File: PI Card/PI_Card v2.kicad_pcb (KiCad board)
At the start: 4 copper layers, 110 x 75 mm, 22 parts, among them J1 Conn_02x20_Odd_Even, J2 Conn_02x20_Odd_Even, J3 Conn_01x03_Pin, J4 Conn_01x02, J5 Conn_02x40_Odd_Even, J6 Conn_01x03_Pin, SW1 SW_Push

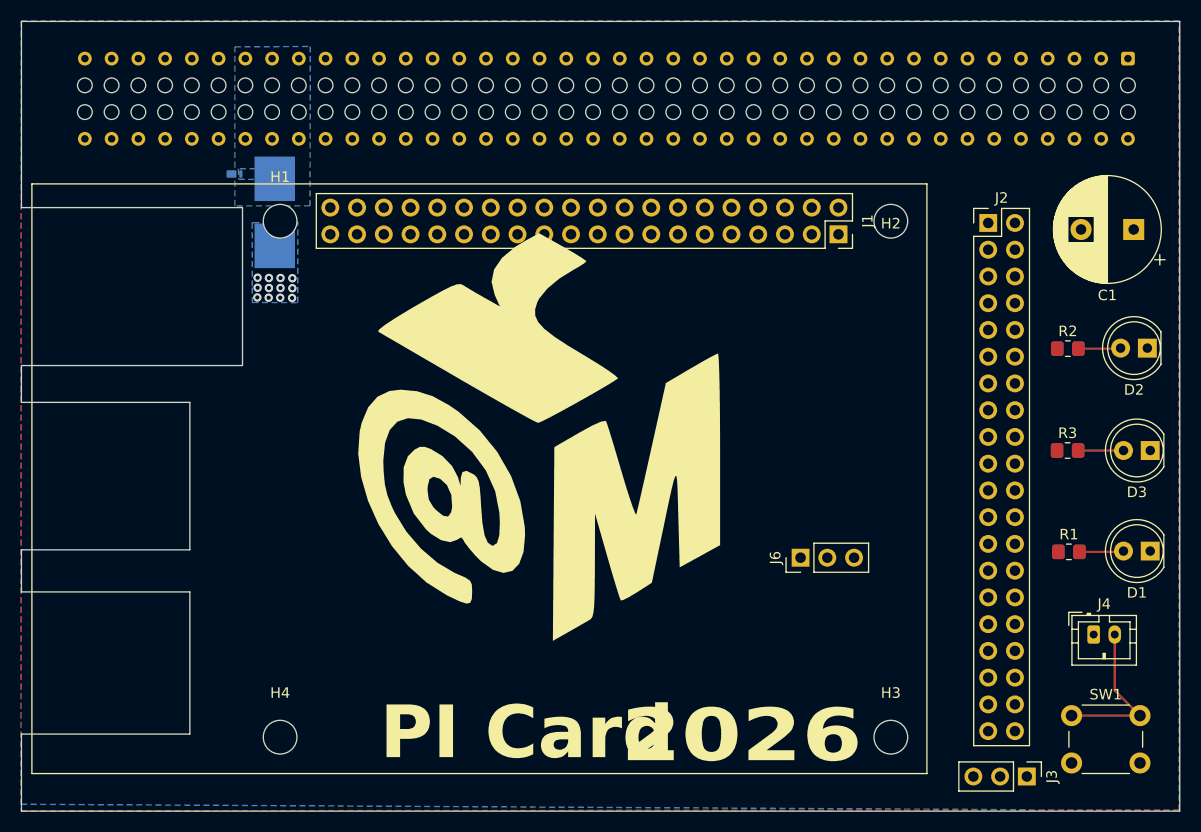
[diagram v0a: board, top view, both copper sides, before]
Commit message: Repositioned Connections
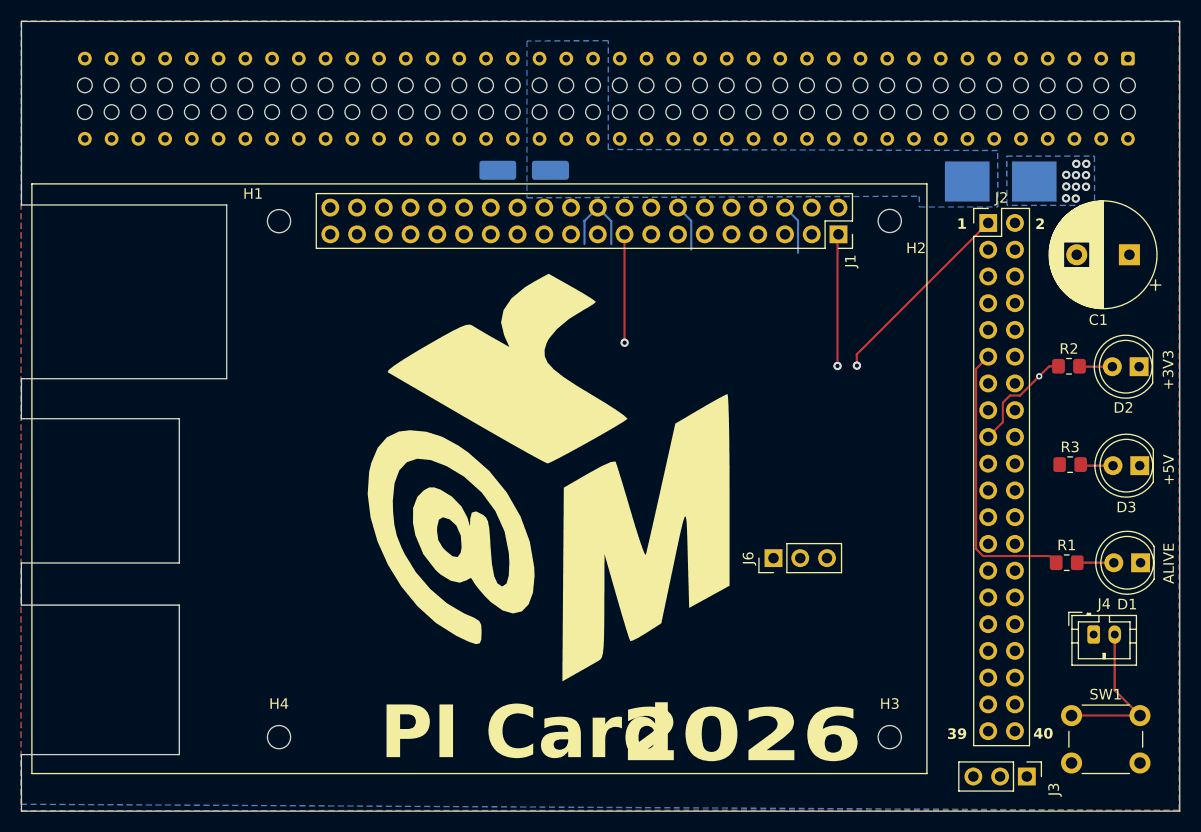
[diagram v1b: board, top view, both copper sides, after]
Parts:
- D4: value PTVS5V0Z1USK -> SMAJ5.0A; footprint Diode_SMD:Nexperia_DSN1608-2_1.6x0.8mm -> Diode_SMD:D_SMA_Handsoldering
- H1, H2, H3, H4: footprint MountingHole:MountingHole_3.2mm_M3 -> MountingHole:MountingHole_2.2mm_M2
- moved F1 69.0 mm to (243.1, 51.7), turned to 180 degrees
- moved D4 27.5 mm to (197.8, 50.6)
- moved G*** 15.0 mm to (200.6, 77.2)
- moved G*** 3.95 mm to (200.2, 79.8)
- moved J6 2.57 mm to (221.5, 87.5)
- moved C1 2.43 mm to (255.3, 58.7)
- moved D2 1.93 mm to (256.2, 69.3)
- moved D3 1.75 mm to (256.3, 78.7)
- moved R2 1.68 mm to (249.6, 69.2)
- moved D1 1.44 mm to (256.4, 87.9)
- moved R3 1.36 mm to (249.7, 78.6)
- moved R1 1.05 mm to (249.4, 87.9)
- moved H2 0.11 mm to (232.6, 55.5)
- moved H1 0.10 mm to (174.6, 55.5)
- moved H3 0.10 mm to (232.6, 104.5)
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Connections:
- J5 pad 1: unconnected-(J5-Pin_1-Pad1) -> GPIO2
- J5 pad 10: GPIO15 -> GPIO24
- J5 pad 11: GPIO17 -> GPIO22
- J5 pad 12: GPIO18 -> GPIO25
- J5 pad 13: GPIO27 -> GPIO10
- J5 pad 14: unconnected-(J5-Pin_14-Pad14) -> GPIO8
- J5 pad 15: GPIO22 -> GPIO9
- J5 pad 16: GPIO23 -> GPIO7
- J5 pad 17: unconnected-(J5-Pin_17-Pad17) -> GPIO11
- J5 pad 18: GPIO24 -> ID_SC
- J5 pad 19: GPIO10 -> ID_SD
- J5 pad 2: unconnected-(J5-Pin_2-Pad2) -> GPIO14
- J5 pad 20: unconnected-(J5-Pin_20-Pad20) -> GPIO12
- J5 pad 21: GPIO9 -> GPIO5
- J5 pad 22: GPIO25 -> GPIO16
- J5 pad 23: GPIO11 -> GPIO6
- J5 pad 24: GPIO8 -> GPIO20
- J5 pad 25: unconnected-(J5-Pin_25-Pad25) -> GPIO13
- J5 pad 26: GPIO7 -> GPIO21
- J5 pad 27: ID_SD -> GPIO19
- J5 pad 28: ID_SC -> unconnected-(J5-Pin_28-Pad28)
- J5 pad 29: GPIO5 -> GPIO26
- J5 pad 3: GPIO2 -> GPIO3
- J5 pad 31: GPIO6 -> unconnected-(J5-Pin_31-Pad31)
- J5 pad 32: GPIO12 -> unconnected-(J5-Pin_32-Pad32)
- J5 pad 33: GPIO13 -> unconnected-(J5-Pin_33-Pad33)
- J5 pad 35: GPIO19 -> unconnected-(J5-Pin_35-Pad35)
- J5 pad 36: GPIO16 -> unconnected-(J5-Pin_36-Pad36)
- J5 pad 37: GPIO26 -> unconnected-(J5-Pin_37-Pad37)
- J5 pad 38: GPIO20 -> unconnected-(J5-Pin_38-Pad38)
- J5 pad 4: unconnected-(J5-Pin_4-Pad4) -> GPIO15
- J5 pad 40: GPIO21 -> unconnected-(J5-Pin_40-Pad40)
- J5 pad 5: GPIO3 -> GPIO4
- J5 pad 6: unconnected-(J5-Pin_6-Pad6) -> GPIO18
- J5 pad 7: GPIO4 -> GPIO17
- J5 pad 8: GPIO14 -> GPIO23
- J5 pad 9: unconnected-(J5-Pin_9-Pad9) -> GPIO27
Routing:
- net +3V3: track 0.00 -> 70.2 mm, vias 0 -> 4
- net GPIO17: track 76.8 -> 111.8 mm
- net GPIO19: track 132.0 -> 152.5 mm
- net GPIO26: track 134.7 -> 154.8 mm
- net GPIO13: track 129.1 -> 149.0 mm
- net GPIO21: track 131.6 -> 150.6 mm
- net GPIO20: track 128.4 -> 146.2 mm
- net GPIO16: track 126.0 -> 143.8 mm
- net GND: track 0.00 -> 17.3 mm
- net GPIO5: track 119.4 -> 134.9 mm
- net GPIO2: track 58.1 -> 43.3 mm
- net GPIO12: track 119.7 -> 134.5 mm
- net GPIO6: track 127.4 -> 141.6 mm
- net ID_SD: track 113.6 -> 126.8 mm
- net GPIO3: track 62.9 -> 49.9 mm
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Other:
- outline, holes or cut-outs redrawn
- board text added: "+3V3"
- board text added: "+5V"
- board text added: "1"
- board text added: "2"
- board text added: "39"
- board text added: "40"
- board text added: "ALIVE"

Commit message: Added I2C & Reset Toggle
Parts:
- added J10: Conn_01x02_Pin, Connector_PinHeader_2.54mm:PinHeader_1x02_P2.54mm_Vertical, F.Cu at (250.9, 66.1)
- added J11: Conn_01x02, Connector_JST:JST_PH_B2B-PH-K_1x02_P2.00mm_Vertical, F.Cu at (248.9, 89.7)
- added J12: Conn_01x02_Pin, Connector_PinHeader_2.54mm:PinHeader_1x02_P2.54mm_Vertical, F.Cu at (257.4, 51.4)
- added J7: Conn_01x02, Connector_JST:JST_PH_B2B-PH-K_1x02_P2.00mm_Vertical, F.Cu at (248.9, 75.4)
- added J8: Conn_01x02, Connector_JST:JST_PH_B2B-PH-K_1x02_P2.00mm_Vertical, F.Cu at (248.9, 96.9)
- added J9: Conn_01x02, Connector_JST:JST_PH_B2B-PH-K_1x02_P2.00mm_Vertical, F.Cu at (248.9, 82.5)
- added SW2: SW_Nidec_CAS-120A1, Button_Switch_SMD:Nidec_Copal_CAS-120A, F.Cu at (255.5, 100.7)
- moved R1 7.45 mm to (255.4, 83.5)
- moved R3 6.23 mm to (255.3, 81.2)
- moved J4 3.01 mm to (254.9, 94.9)
- moved D3 2.11 mm to (256.9, 76.7)
- moved SW1 2.10 mm to (249.8, 104.5)
- moved D2 1.20 mm to (257.3, 68.7)
- moved C1 1.11 mm to (256.4, 59.1)
- moved D1 0.87 mm to (257.2, 88.1)
- moved R2 0.40 mm to (249.2, 69.2)
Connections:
- J4 pad 2: RUN -> Net-(J4-Pin_2)
- SW1 pad 1: RUN -> Net-(J4-Pin_2)
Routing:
- net GND: track 17.3 -> 88.4 mm
- net SCL: track 0.00 -> 54.6 mm
- net SDA: track 0.00 -> 35.5 mm
- net GLOBAL_EN: track 28.2 -> 45.4 mm, vias 0 -> 1
- net Net-(J4-Pin_2): track 0.00 -> 17.1 mm
- net GPIO2: track 43.3 -> 59.0 mm
- net GPIO3: track 49.9 -> 58.9 mm
- net RUN: track 63.5 -> 58.5 mm, vias 0 -> 1
- net Net-(D3-A): track 3.13 -> 5.39 mm
- net Net-(D1-A): track 3.48 -> 5.26 mm
- net Net-(D2-A): track 3.14 -> 4.86 mm
- net GPIO17: track 111.8 -> 113.2 mm
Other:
- board text added: "Global Enable"
- board text added: "RUN"

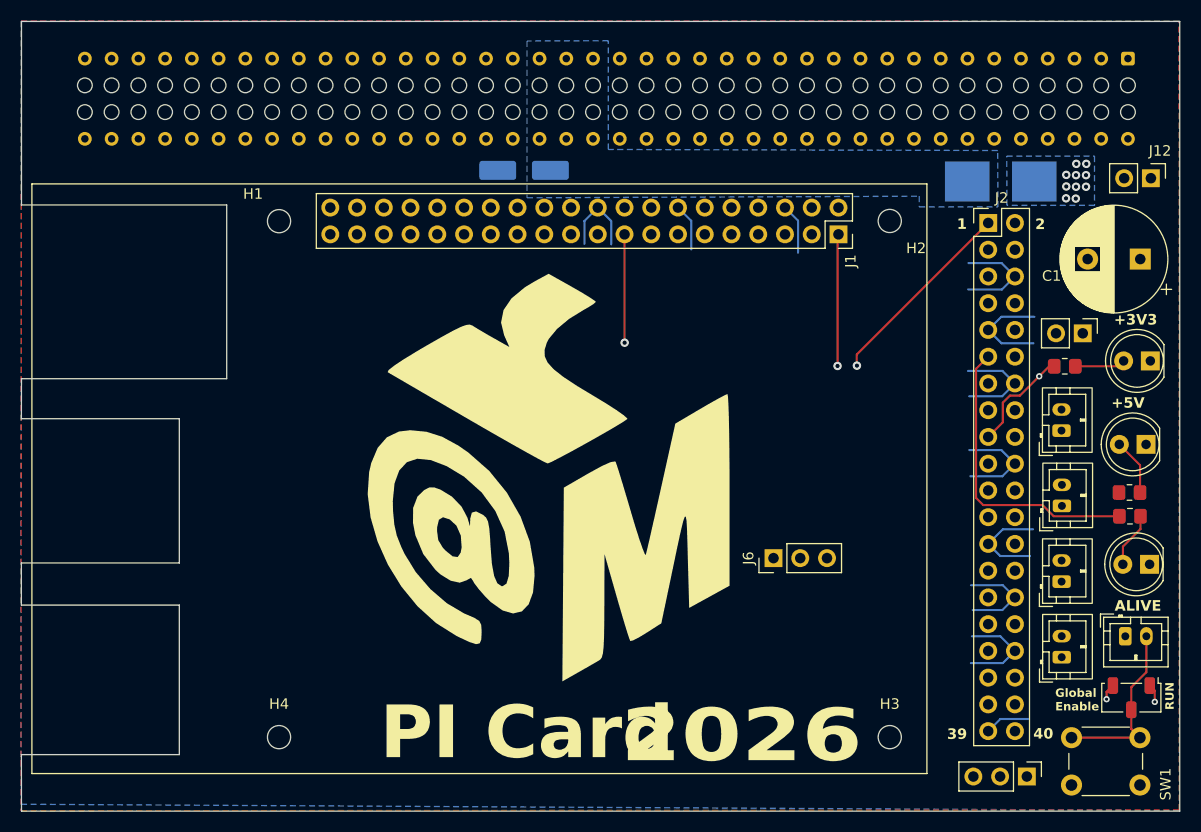
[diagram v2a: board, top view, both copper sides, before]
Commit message: Cut off Arms
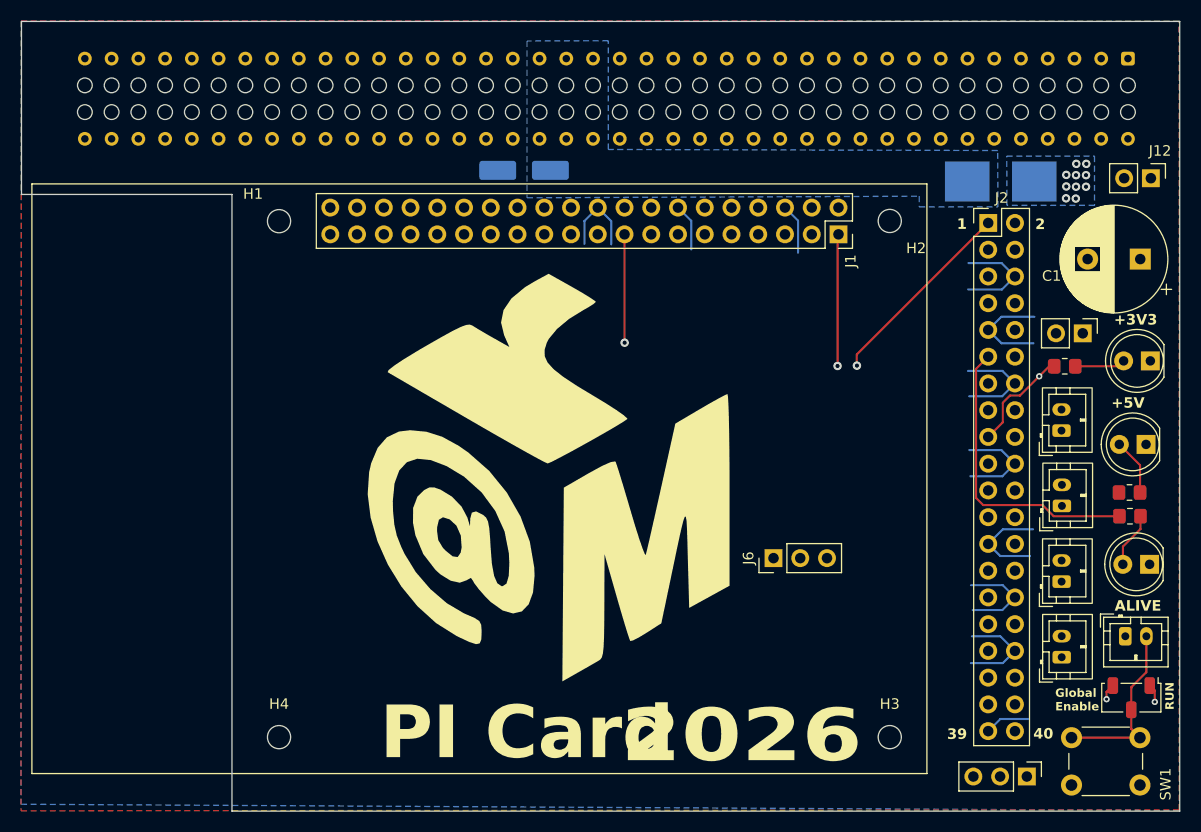
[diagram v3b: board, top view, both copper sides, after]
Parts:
- moved G*** 2.82 mm to (203.5, 77.3)
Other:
- outline, holes or cut-outs redrawn
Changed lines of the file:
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@@
 	(footprint "LOGO"
 		(layer "B.Cu")
-		(at 200.637294 77.183531 180)
+		(at 203.457294 77.313531 180)
 		(property "Reference" "G***"
 			(at 0 0 0)
@@
 	)
 	(gr_line
-		(start 165.09 87.93)
-		(end 165.09 74.23)
-		(stroke
-			(width 0.05)
-			(type default)
-		)
-		(layer "Edge.Cuts")
-	)
-	(gr_line
-		(start 165.09 74.23)
-		(end 150.09 74.23)
-		(stroke
-			(width 0.05)
-			(type default)
-		)
-		(layer "Edge.Cuts")
-	)
-	(gr_line
-		(start 150.090019 106.130222)
-		(end 150.1 111.5)
-		(stroke
-			(width 0.05)
-			(type default)
-		)
-		(layer "Edge.Cuts")
-	)
-	(gr_line
-		(start 165.09 91.93)
-		(end 165.09 106.13)
-		(stroke
-			(width 0.05)
-			(type default)
-		)
-		(layer "Edge.Cuts")
-	)
-	(gr_line
 		(start 260.1 36.5)
 		(end 150.1 36.5)
@@
 	)
 	(gr_line
-		(start 169.59 53.93)
-		(end 169.59 70.43)
-		(stroke
-			(width 0.05)
-			(type default)
-		)
-		(layer "Edge.Cuts")
-	)
-	(gr_line
-		(start 165.09 87.93)
-		(end 150.09 87.93)
+		(start 170.09 52.93)
+		(end 170.09 111.5)
 		(stroke
 			(width 0.05)
@@
 	)
 	(gr_line
-		(start 150.1 111.5)
+		(start 170.09 111.5)
 		(end 260.1 111.5)
 		(stroke
@@
 	)
 	(gr_line
-		(start 150.1 53.93)
-		(end 169.59 53.93)
+		(start 150.1 52.93)
+		(end 170.09 52.93)
 		(stroke
 			(width 0.05)
@@
 	(gr_line
 		(start 150.1 36.5)
-		(end 150.1 53.93)
-		(stroke
-			(width 0.05)
-			(type default)
-		)
-		(layer "Edge.Cuts")
-	)
-	(gr_line
-		(start 150.1 70.43)
-		(end 169.59 70.43)
-		(stroke
-			(width 0.05)
-			(type default)
-		)
-		(layer "Edge.Cuts")
-	)
-	(gr_line
-		(start 150.1 70.43)
-		(end 150.09 74.23)
-		(stroke
-			(width 0.05)
-			(type default)
-		)
-		(layer "Edge.Cuts")
-	)
-	(gr_line
-		(start 165.09 106.13)
-		(end 150.09 106.13)
-		(stroke
-			(width 0.05)
-			(type default)
-		)
-		(layer "Edge.Cuts")
-	)
-	(gr_line
-		(start 165.09 91.93)
-		(end 150.09 91.93)
-		(stroke
-			(width 0.05)
-			(type default)
-		)
-		(layer "Edge.Cuts")
-	)
-	(gr_line
-		(start 150.09 87.93)
-		(end 150.09 91.93)
+		(end 150.1 52.93)
 		(stroke
 			(width 0.05)
